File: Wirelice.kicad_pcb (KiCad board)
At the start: 2 copper layers, 337.4 x 122.5 mm, 185 parts, among them J1 SWD, J2 USB_C_Receptacle_USB2.0, J3 Unified DB, J5 Battery, Q1 2N7002, Q2 AO3401A, SW29 SW_Push, U1 nRF52840_holyiot_18010, U2 SRV05-4, U3 TP4056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

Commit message: Removed LEDS and updated holes
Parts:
- removed C10, C2, C4, C6: 100nF, Capacitor_SMD:C_0603_1608Metric
- removed D2, D4: SK6812MINI, LED_SMD:LED_SK6812MINI_PLCC4_3.5x3.5mm_P1.75mm
- removed Q1: 2N7002, Package_TO_SOT_SMD:SOT-23
- removed Q2: AO3401A, Package_TO_SOT_SMD:SOT-23
- removed R10, R11, R9: 10k, Resistor_SMD:R_0603_1608Metric
- removed R6: 100R, Resistor_SMD:R_0603_1608Metric
- removed U7: TXS0101, Package_TO_SOT_SMD:SOT-363_SC-70-6
- moved SW29 11.1 mm to (197.2, 123.4)
- moved R12 3.56 mm to (205.7, 101.0)
- moved R13 3.56 mm to (207.3, 101.0)
- moved D64 0.54 mm to (43.0, 181.7)
- moved D65 0.54 mm to (43.0, 177.2)
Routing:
- net GND: track 282.8 -> 187.7 mm, vias 31 -> 27
- net UG_PWR: track 66.8 -> 0.00 mm
- net Net-(D2-Pad1): track 36.5 -> 0.00 mm
- net UG_HV: track 26.6 -> 0.00 mm
- net UG_LV: track 19.3 -> 0.00 mm, vias 2 -> 0
- net Net-(Q1-Pad3): track 11.7 -> 0.00 mm, vias 2 -> 0
- net /RESET: track 7.09 -> 18.4 mm
- net +3V3: track 30.4 -> 20.5 mm, vias 4 -> 2
- net VBAT: track 78.8 -> 70.3 mm
- net UG_EN: track 5.51 -> 0.00 mm
- net /CHRG: track 7.60 -> 2.65 mm
- net /STDBY: track 7.71 -> 2.75 mm
- net Net-(Q1-Pad1): track 3.94 -> 0.00 mm
- net Net-(R11-Pad1): track 2.85 -> 0.00 mm
- net Net-(D64-Pad1): track 256.4 -> 258.2 mm
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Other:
- board size 337.4 x 122.5 mm -> 337.8 x 122.5 mm

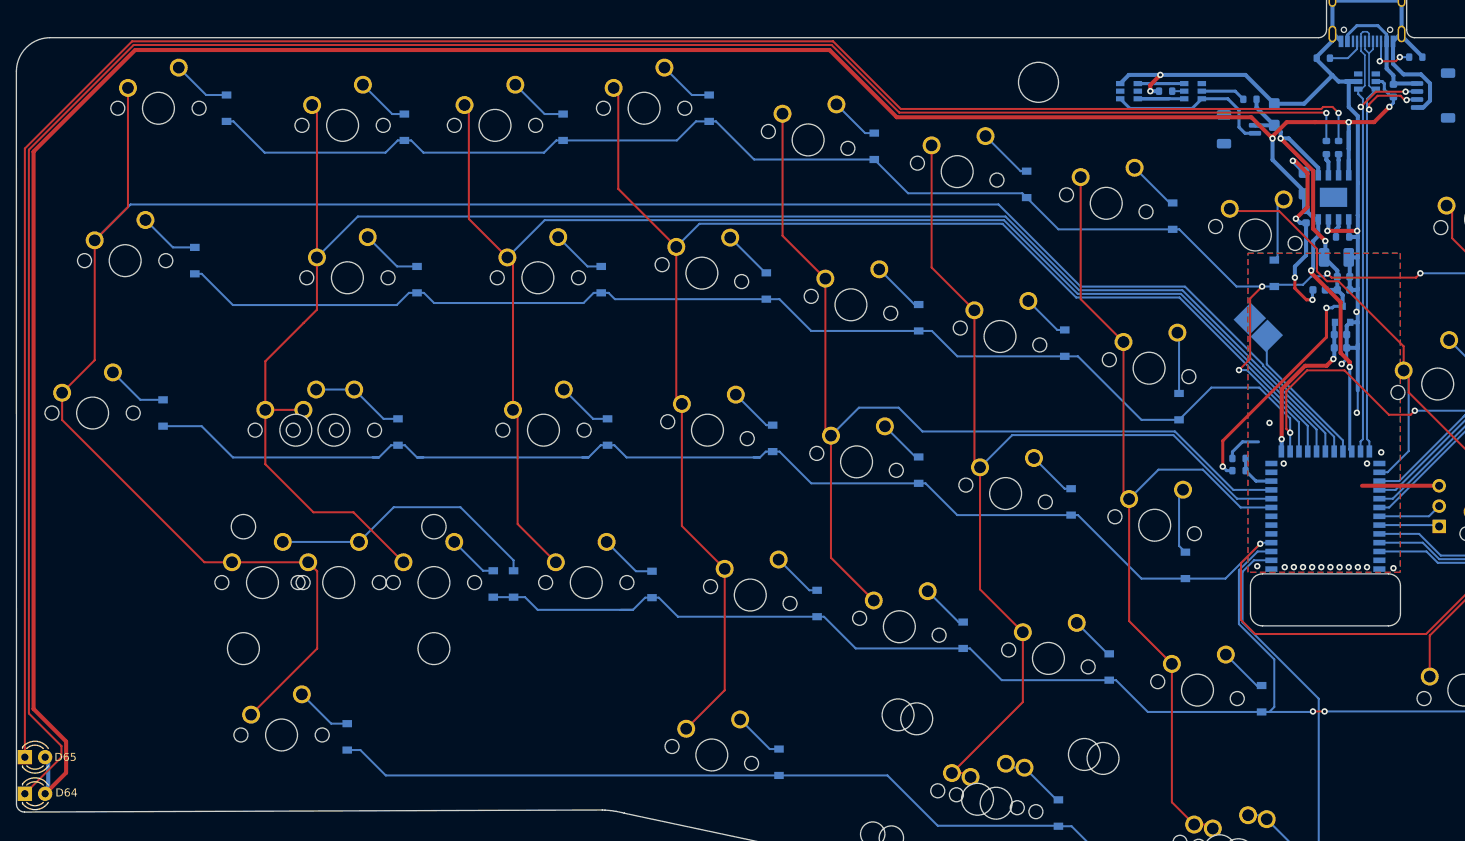
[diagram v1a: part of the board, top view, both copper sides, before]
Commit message: Compacted components and removed RGBs
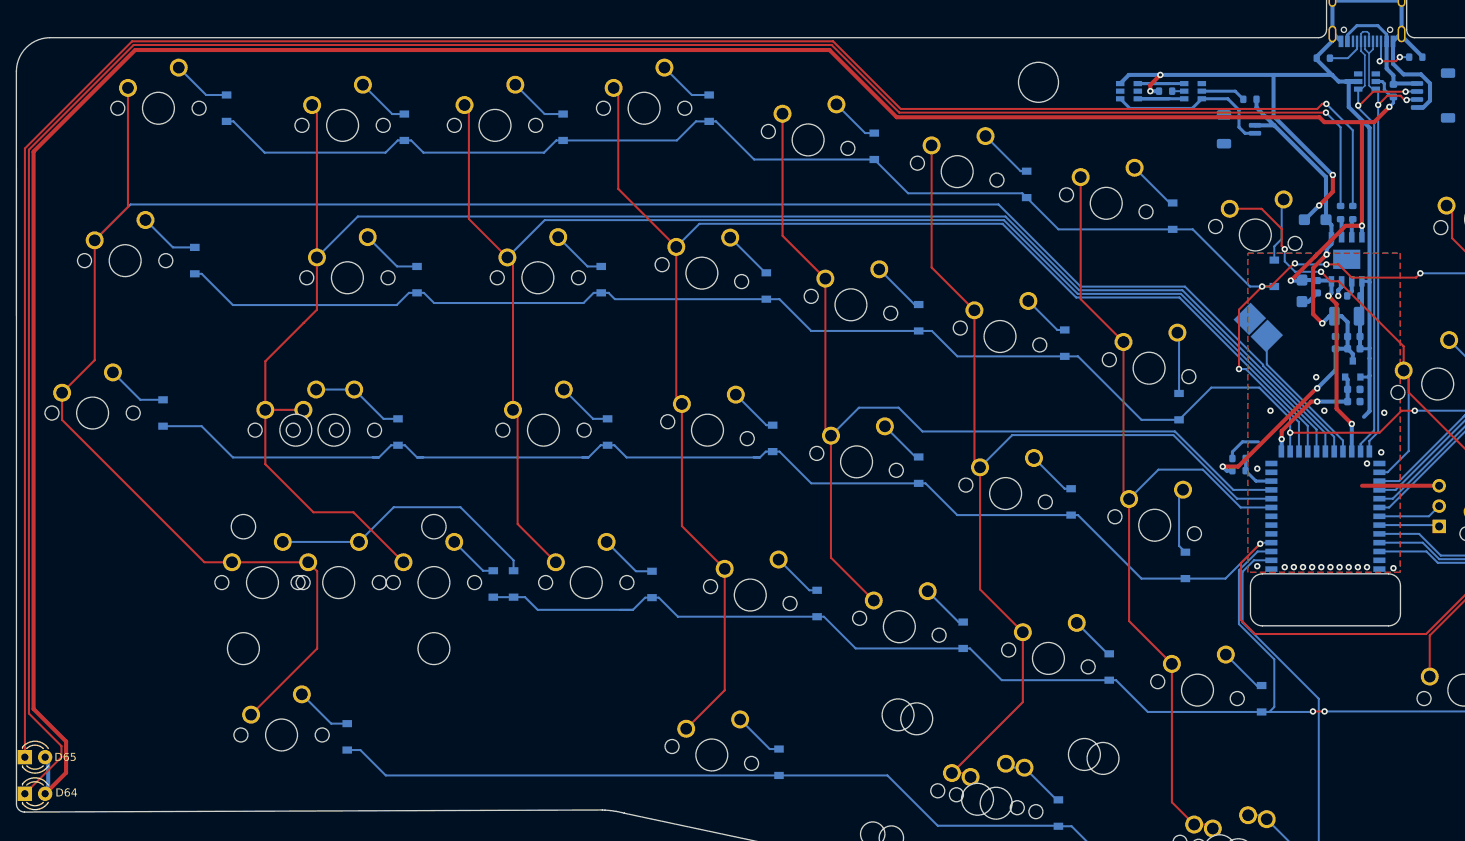
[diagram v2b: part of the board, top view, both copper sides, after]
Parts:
- added H1: MountingHole, sleep-lib:noun_geometric pattern_889496, B.Cu at (342.9, 173.9)
- moved C14 14.1 mm to (204.3, 110.0), turned to 180 degrees
- moved C11 13.5 mm to (202.7, 118.9), turned to -90 degrees
- moved C12 8.87 mm to (204.6, 118.4)
- moved R12 8.32 mm to (207.5, 109.1)
- moved R13 8.32 mm to (209.0, 109.1)
- moved U3 7.92 mm to (208.3, 114.9)
- moved C21 7.59 mm to (209.2, 124.6)
- moved R3 7.50 mm to (209.2, 119.5)
- moved C22 7.46 mm to (209.2, 126.1)
- moved C18 7.46 mm to (208.3, 122.0)
- moved C23 7.04 mm to (209.2, 131.2)
- moved U6 6.96 mm to (209.0, 128.7)
- moved C24 6.92 mm to (209.2, 132.7)
- moved C20 6.90 mm to (206.9, 125.3), turned to -90 degrees
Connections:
- U1 pad 12: UG_EN -> unconnected-(U1-Pad12)
- U1 pad 13: UG_LV -> unconnected-(U1-Pad13)
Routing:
- net GND: track 187.7 -> 175.8 mm, vias 27 -> 24
- net Net-(D65-Pad1): track 253.0 -> 262.0 mm
- net Net-(D64-Pad1): track 258.2 -> 267.0 mm
- net ROW1: track 339.9 -> 331.5 mm
- net +3V3: track 20.5 -> 15.5 mm
- net +5V: track 328.2 -> 325.3 mm
- net ROW0: track 350.7 -> 353.3 mm, vias 4 -> 5
- net D+: track 61.7 -> 59.9 mm
- net D-: track 63.4 -> 64.4 mm
- net COL7: track 93.6 -> 94.5 mm, vias 0 -> 2
- net VBAT: track 70.3 -> 69.4 mm
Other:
- board text added: "Connect Pads For Reset"
- board text added: "Wirelice Designed by Sleepdealer"

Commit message: Updated things
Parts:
- added C1: 100nF, Capacitor_SMD:C_0603_1608Metric, B.Cu at (192.3, 94.1)
- added FB1: Ferrite Bead, Inductor_SMD:L_0805_2012Metric, B.Cu at (206.2, 90.8)
- added SW1: Rotary_Encoder_Switch, Keeb-IO:RotaryEncoder_Alps_EC11E-Switch_Vertical_H20mm, F.Cu at (59.7, 96.0)
- D64, D65: footprint LED_THT:LED_D3.0mm -> LED_SMD:LED_0805_2012Metric; moved to B.Cu
- H1: value MountingHole -> Logo; footprint sleep-lib:noun_geometric pattern_889496 -> sleep-lib:logo-large-CU
- J5: footprint Connector_JST:JST_SH_SM02B-SRSS-TB_1x02-1MP_P1.00mm_Horizontal -> Connector_JST:JST_PH_S2B-PH-SM4-TB_1x02-1MP_P2.00mm_Horizontal
- U3: footprint sleep-lib:SOP-8 -> Package_SO:SOIC-8-1EP_3.9x4.9mm_P1.27mm_EP2.29x3mm
- moved D64 181.1 mm to (207.3, 105.4), turned to 90 degrees
- moved D65 181.1 mm to (209.3, 105.4), turned to 90 degrees
- moved J1 5.18 mm to (220.1, 143.1), turned to 180 degrees
- moved J5 4.37 mm to (190.8, 100.5)
- moved R1 2.17 mm to (203.3, 90.6), turned to -90 degrees
- moved SW29 1.09 mm to (196.2, 123.8)
- turned C18 to 0 degrees
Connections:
- net Net-(R3-Pad1) renamed /PROG
- net Net-(R5-Pad1) renamed /CSI
- net Net-(U4-Pad4) renamed /OC
- net Net-(U4-Pad6) renamed /OD
- C18 pad 1: GND -> VBAT
- C18 pad 2: VBAT -> GND
- J1 pad 1: /SWDIO -> GND
- J1 pad 3: GND -> /SWDIO
- J2 pad S1: GND -> GNDPWR
- U1 pad 10: COL4 -> ENCB
- U1 pad 36: unconnected-(U1-Pad36) -> EXTRA4
- U1 pad 6: unconnected-(U1-Pad6) -> COL6
- U1 pad 7: unconnected-(U1-Pad7) -> COL5
- U1 pad 8: COL6 -> COL4
- U1 pad 9: COL5 -> ENCA
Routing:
- net Net-(D64-Pad1): track 267.0 -> 2.07 mm, vias 1 -> 0
- net Net-(D65-Pad1): track 262.0 -> 2.07 mm, vias 1 -> 0
- net +5V: track 325.3 -> 65.8 mm, vias 5 -> 6
- net ENCA: track 0.00 -> 165.0 mm, vias 0 -> 1
- net ENCB: track 0.00 -> 159.1 mm, vias 0 -> 1
- net GND: track 175.8 -> 276.3 mm, vias 24 -> 27
- net GNDPWR: track 0.00 -> 20.6 mm
- net VBAT: track 69.4 -> 74.4 mm
- net COL0: track 276.7 -> 281.6 mm
- net /OD: track 9.74 -> 5.80 mm
- net /OC: track 9.74 -> 5.80 mm
- net /CC1: track 4.82 -> 7.70 mm, vias 0 -> 2
- net Net-(D15-Pad2): track 7.39 -> 9.33 mm
- net Net-(C1-Pad1): track 20.9 -> 22.4 mm
- net D+: track 59.9 -> 61.4 mm
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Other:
- board size 337.8 x 122.5 mm -> 337.7 x 122.7 mm
- board text added: "+"
- board text added: "-"
- board text added: "Battery"
- board text added: "CHARGING ▼"
- board text added: "Daughterboard"
- board text added: "JLCJLCJLCJLC"
- board text added: "STANDBY ▼"
